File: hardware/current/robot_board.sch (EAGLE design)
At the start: 150 parts, among them J1 POWER_JACKPTH, Q1 DMP2035U, Q2 DMP2035U, Q3 DMP2035U-7, Q4 DMP2035U-7, Q5 DMP2035U, U1 FT232RL-BASICSSOP, U10 DRV8839, U12 LM393, U16 LM393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

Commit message: USB and main power are switched with on/off switch
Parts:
- removed D33: BAT54C, diode:BAT54C
- removed Q5: DMP2035U, jseng:DMP2035U
- added C13: 22uF, resistor:C-USC1206
- added R29: 330, resistor:R-US_R1206
- added R32: 20K 1%, resistor:R-US_R1206
- added R33: 300, resistor:R-US_R1206
- added U$5: AP431SAG-7, jseng:AP431SAG-7
- added U$6, U$7: SIA907EDJT, jseng:SIA907EDJT
- D23: value 2.4V -> RX; device SparkFun-DiscreteSemi:DIODESOT23 -> SparkFun-LED:LED-GREENLILYPAD
- JP4: device SparkFun-Connectors:M06SIP -> SparkFun-Connectors:M081X08
- R23: value 1K 1% -> 10K 1%
- R24: value 27K 1% -> 24K 1%
- R31: value 20K 1% -> 24K 1%
- R34: value 20K 1% -> 300
- R35: value 5.11K 1% -> 120K 1%
- R36: value 20K 1% -> 600K 1%
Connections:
- removed net 2.4V: D23.C, R23.1, U12G1.-IN, U12G2.-IN, U16G1.-IN
- removed net N$33: F1.2, JP4.6, Q1.D
- removed net N$36: Q1.G, R34.2
- new net 2.5V: R23.1, U$5.CATHODE, U$5.REF, U12G1.-IN, U12G2.-IN, U16G1.-IN
- new net N$22: D23.C, U1.TXLED
- new net N$23: U$7.D1, U$7.D2
- new net N$24: U$6.D1, U$6.D2
- new net N$25: R33.2, U$1.6
- new net N$26: R34.1, U$1.9
- new net PWR_GATE: Q1.D, R32.2, U$6.G1, U$6.G2
- new net VIN1: D24.A1, F1.2, U$6.S1
- net 3V3_OUT: now also JP4.4; no longer JP4.2
- net 5V: now also R29.1, U12G1.V+
- net 5V_OUT: now also JP4.5; no longer JP4.3
- net GND: now also C13.2, JP4.6, JP4.7, R32.1, U$5.ANODE; no longer D23.A, JP4.4, JP4.5, R34.1
- net LCD0: now also R34.2; no longer U$1.9
- net N$12: now also D23.A, R29.2; no longer D33.CC, R42.2
- net N$18: now also Q1.S, R42.2
- net N$7: now also JP4.3; no longer JP4.1
- net PWR_SW: now also U$6.S2, U$7.S2; no longer D33.A1, Q1.S, Q5.D
- net RS: now also R33.1; no longer U$1.6
- net USBGATE: now also Q1.G, U$7.G1, U$7.G2; no longer Q5.G, U$3.EN
- net USB_5V: now also U$7.S1; no longer D33.A2, Q5.S
- net VIN: now also R35.2
- net VIN_F: now also C13.1, JP4.8, U$3.EN; no longer D24.A1, R35.2, U12G1.V+
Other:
- note removed: "Reverse Polarity Protection"
- moved on the sheet: D24, F1, J1, Q1, R23, R28, R34, R35, R36, R42, U16G1, U16G2

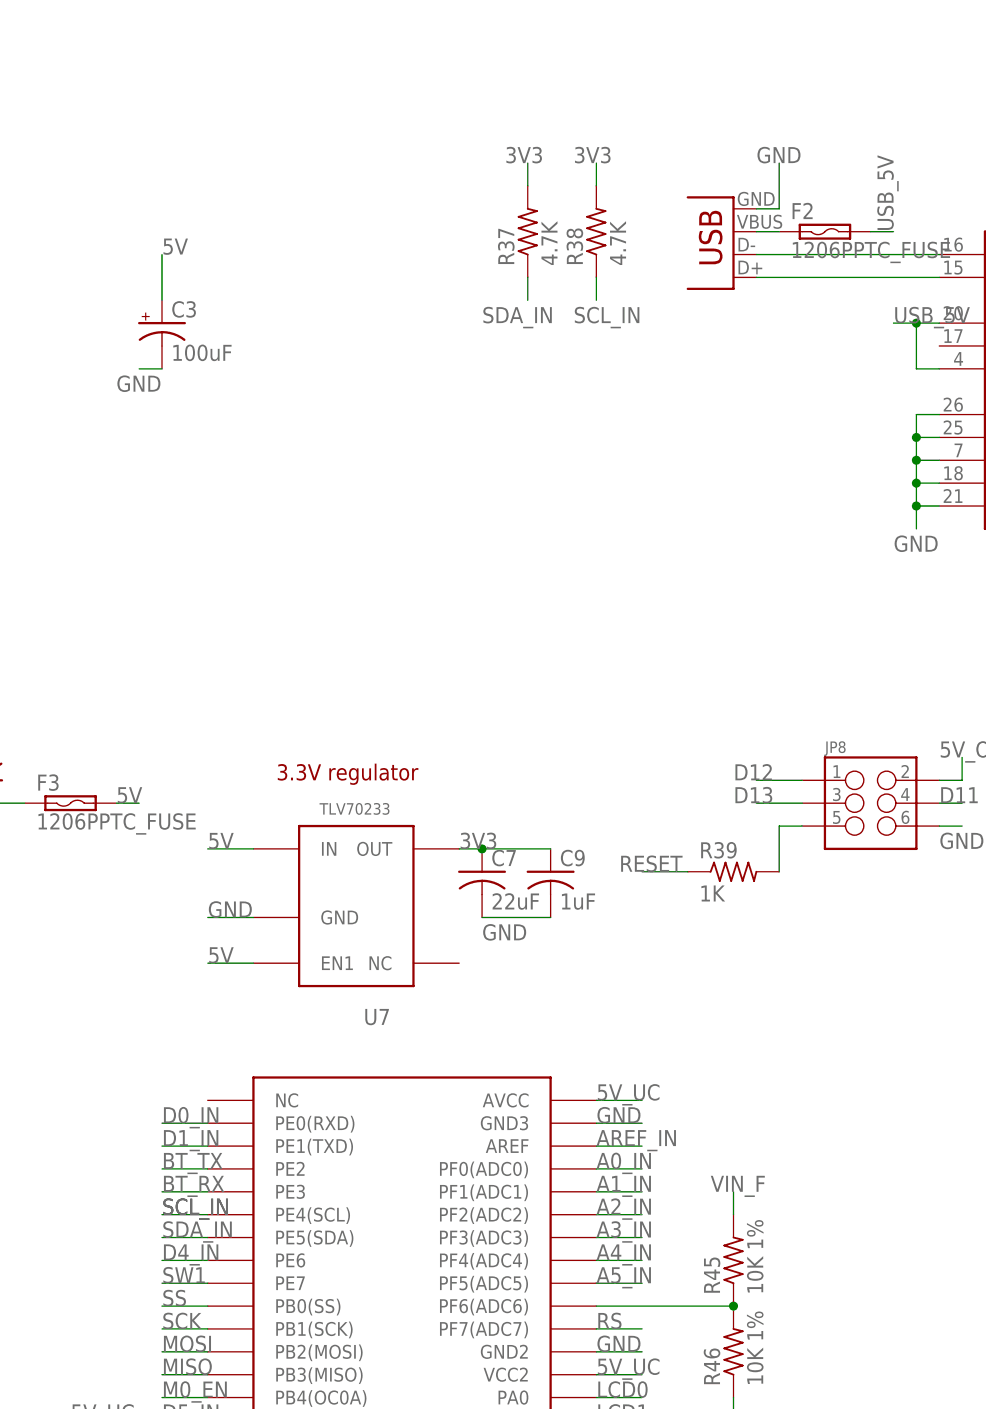
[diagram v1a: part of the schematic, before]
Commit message: added i2c level shifter
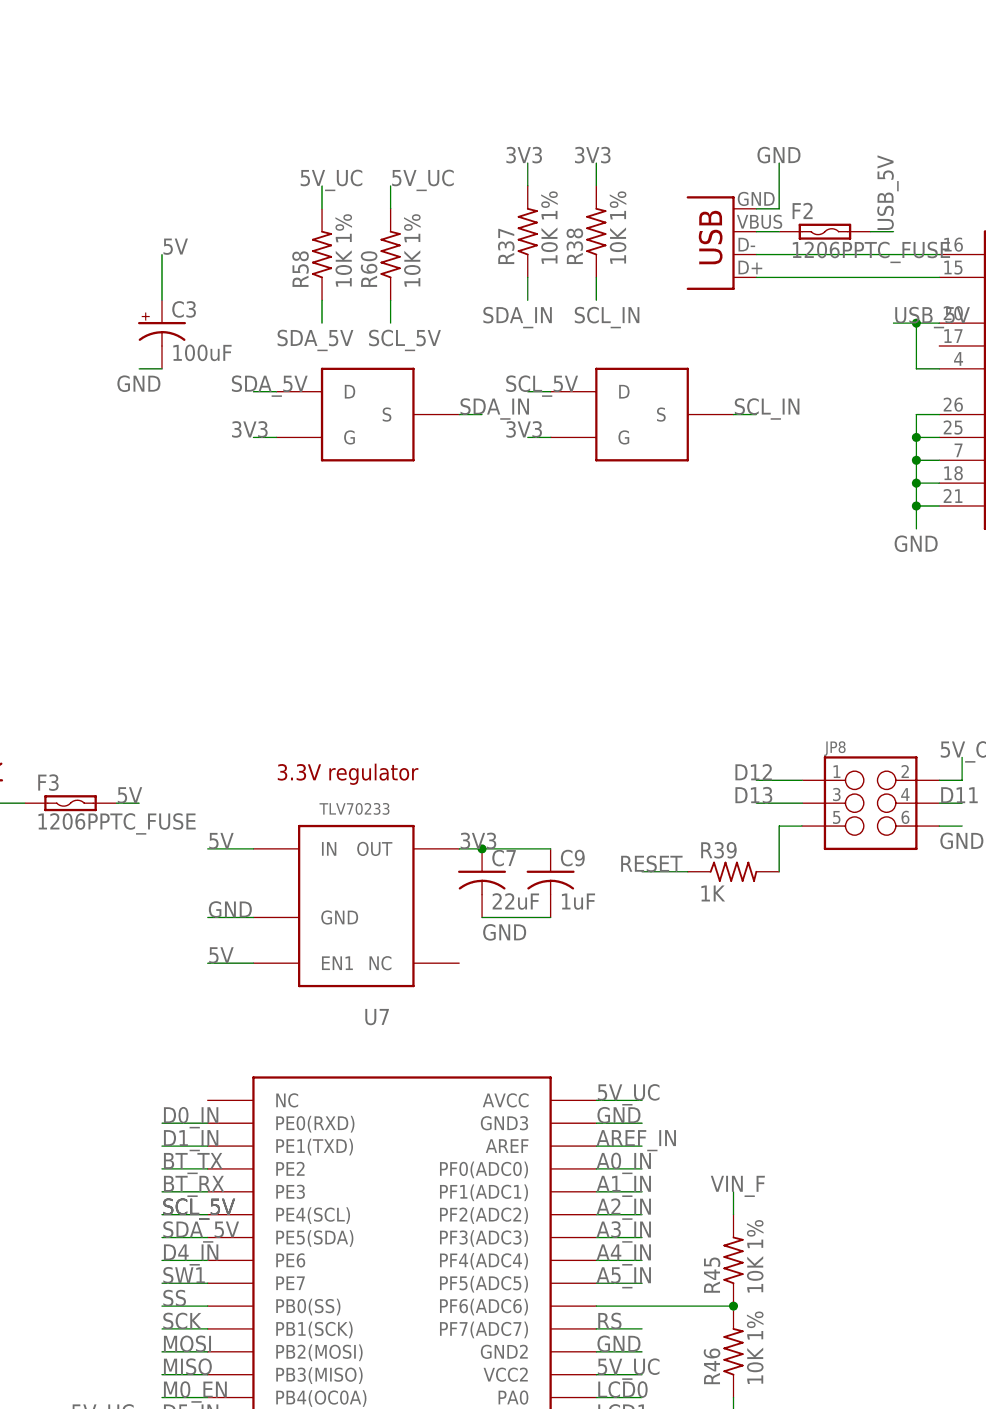
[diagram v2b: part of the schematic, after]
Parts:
- added R58, R60: 10K 1%, resistor:R-US_R1206
- added U$10, U$9: BSS138, jseng:BSS138
- R37, R38: value 4.7K -> 10K 1%
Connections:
- new net SCL_5V: R60.1, U$10.D, U17.PE4(SCL)
- new net SDA_5V: R58.1, U$9.D, U17.PE5(SDA)
- net 3V3: now also U$10.G, U$9.G
- net 5V_UC: now also R58.2, R60.2
- net SCL_IN: now also U$10.S; no longer U17.PE4(SCL)
- net SDA_IN: now also U$9.S; no longer U17.PE5(SDA)
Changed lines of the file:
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@@
 <part name="R30" library="resistor" deviceset="R-US_" device="R1206" value="20K 1%"/>
 <part name="R31" library="resistor" deviceset="R-US_" device="R1206" value="24K 1%"/>
-<part name="R37" library="resistor" deviceset="R-US_" device="R1206" value="4.7K"/>
-<part name="R38" library="resistor" deviceset="R-US_" device="R1206" value="4.7K"/>
+<part name="R37" library="resistor" deviceset="R-US_" device="R1206" value="10K 1%"/>
+<part name="R38" library="resistor" deviceset="R-US_" device="R1206" value="10K 1%"/>
 <part name="C4" library="resistor" deviceset="C-US" device="C1206" value=".1uF"/>
 <part name="R40" library="resistor" deviceset="R-US_" device="R1206" value="10K 1%"/>
@@
 <part name="R34" library="resistor" deviceset="R-US_" device="R1206" value="300"/>
 <part name="JP4" library="SparkFun-Connectors" deviceset="M08" device="1X08"/>
+<part name="R58" library="resistor" deviceset="R-US_" device="R1206" value="10K 1%"/>
+<part name="R60" library="resistor" deviceset="R-US_" device="R1206" value="10K 1%"/>
+<part name="U$9" library="jseng" deviceset="BSS138" device=""/>
+<part name="U$10" library="jseng" deviceset="BSS138" device=""/>
 </parts>
 <sheets>
@@
 <instance part="R34" gate="G$1" x="320.04" y="91.44" rot="R90"/>
 <instance part="JP4" gate="G$1" x="233.68" y="-45.72" rot="R180"/>
+<instance part="R58" gate="G$1" x="124.46" y="167.64" rot="R90"/>
+<instance part="R60" gate="G$1" x="132.08" y="167.64" rot="R90"/>
+<instance part="U$9" gate="G$1" x="129.54" y="149.86"/>
+<instance part="U$10" gate="G$1" x="160.02" y="149.86"/>
 </instances>
 <busses>
@@
 <label x="327.66" y="12.7" size="1.778" layer="95"/>
 </segment>
+<segment>
+<pinref part="U$9" gate="G$1" pin="G"/>
+<wire x1="119.38" y1="147.32" x2="116.84" y2="147.32" width="0.1524" layer="91"/>
+<label x="114.3" y="147.32" size="1.778" layer="95"/>
+</segment>
+<segment>
+<pinref part="U$10" gate="G$1" pin="G"/>
+<wire x1="149.86" y1="147.32" x2="147.32" y2="147.32" width="0.1524" layer="91"/>
+<label x="144.78" y="147.32" size="1.778" layer="95"/>
+</segment>
 </net>
 <net name="RESET" class="0">
@@
 <wire x1="335.28" y1="81.28" x2="332.74" y2="81.28" width="0.1524" layer="91"/>
 <label x="332.74" y="81.28" size="1.778" layer="95"/>
+</segment>
+<segment>
+<pinref part="R58" gate="G$1" pin="2"/>
+<wire x1="124.46" y1="172.72" x2="124.46" y2="175.26" width="0.1524" layer="91"/>
+<label x="121.92" y="175.26" size="1.778" layer="95"/>
+</segment>
+<segment>
+<pinref part="R60" gate="G$1" pin="2"/>
+<wire x1="132.08" y1="172.72" x2="132.08" y2="175.26" width="0.1524" layer="91"/>
+<label x="132.08" y="175.26" size="1.778" layer="95"/>
 </segment>
 </net>
@@
 <net name="SCL_IN" class="0">
 <segment>
-<pinref part="U17" gate="G$1" pin="PE4(SCL)"/>
-<wire x1="111.76" y1="60.96" x2="106.68" y2="60.96" width="0.1524" layer="91"/>
-<label x="106.68" y="60.96" size="1.778" layer="95"/>
-<label x="106.68" y="60.96" size="1.778" layer="95"/>
-</segment>
-<segment>
 <pinref part="D7" gate="G$1" pin="C"/>
 <pinref part="R7" gate="G$1" pin="1"/>
@@
 <label x="312.42" y="116.84" size="1.778" layer="95"/>
 </segment>
+<segment>
+<pinref part="U$10" gate="G$1" pin="S"/>
+<wire x1="170.18" y1="149.86" x2="172.72" y2="149.86" width="0.1524" layer="91"/>
+<label x="170.18" y="149.86" size="1.778" layer="95"/>
+</segment>
 </net>
 <net name="SDA_IN" class="0">
-<segment>
-<pinref part="U17" gate="G$1" pin="PE5(SDA)"/>
-<wire x1="111.76" y1="58.42" x2="106.68" y2="58.42" width="0.1524" layer="91"/>
-<label x="106.68" y="58.42" size="1.778" layer="95"/>
-</segment>
 <segment>
 <pinref part="D8" gate="G$1" pin="C"/>
@@
 <wire x1="332.74" y1="104.14" x2="325.12" y2="104.14" width="0.1524" layer="91"/>
 <label x="322.58" y="104.14" size="1.778" layer="95"/>
+</segment>
+<segment>
+<pinref part="U$9" gate="G$1" pin="S"/>
+<wire x1="139.7" y1="149.86" x2="142.24" y2="149.86" width="0.1524" layer="91"/>
+<label x="139.7" y="149.86" size="1.778" layer="95"/>
 </segment>
 </net>
@@
 </segment>
 </net>
+<net name="SCL_5V" class="0">
+<segment>
+<pinref part="U$10" gate="G$1" pin="D"/>
+<wire x1="149.86" y1="152.4" x2="147.32" y2="152.4" width="0.1524" layer="91"/>
+<label x="144.78" y="152.4" size="1.778" layer="95"/>
+</segment>
+<segment>
+<pinref part="R60" gate="G$1" pin="1"/>
+<wire x1="132.08" y1="162.56" x2="132.08" y2="160.02" width="0.1524" layer="91"/>
+<label x="129.54" y="157.48" size="1.778" layer="95"/>
+</segment>
+<segment>
+<pinref part="U17" gate="G$1" pin="PE4(SCL)"/>
+<wire x1="111.76" y1="60.96" x2="106.68" y2="60.96" width="0.1524" layer="91"/>
+<label x="106.68" y="60.96" size="1.778" layer="95"/>
+<label x="106.68" y="60.96" size="1.778" layer="95"/>
+</segment>
+</net>
+<net name="SDA_5V" class="0">
+<segment>
+<pinref part="U$9" gate="G$1" pin="D"/>
+<wire x1="119.38" y1="152.4" x2="116.84" y2="152.4" width="0.1524" layer="91"/>
+<label x="114.3" y="152.4" size="1.778" layer="95"/>
+</segment>
+<segment>
+<pinref part="R58" gate="G$1" pin="1"/>
+<wire x1="124.46" y1="162.56" x2="124.46" y2="160.02" width="0.1524" layer="91"/>
+<label x="119.38" y="157.48" size="1.778" layer="95"/>
+</segment>
+<segment>
+<pinref part="U17" gate="G$1" pin="PE5(SDA)"/>
+<wire x1="111.76" y1="58.42" x2="106.68" y2="58.42" width="0.1524" layer="91"/>
+<label x="106.68" y="58.42" size="1.778" layer="95"/>
+</segment>
+</net>

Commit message: revision 2
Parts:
- added JP12: M02PTH, SparkFun-Connectors:M02PTH
- added U$11: BSS138, jseng:BSS138
- R23: value 10K 1% -> 20K 1%
- U$1: value M08X2 -> 2X7HEADER; device SparkFun-Connectors:M08X2 -> jseng:2X7HEADER
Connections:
- new net ACCEL_INT1: U$11.G, U$8.INT1
- net 5V: now also U$1.P$2; no longer U$1.4
- net 5V_OUT: now also JP4.2
- net ACCEL_INT: now also U$11.D; no longer U$8.INT1
- net E: now also U$1.P$6; no longer U$1.8
- net GND: now also U$1.P$1, U$1.P$5, U$11.S; no longer U$1.3, U$1.7
- net LCD1: now also U$1.P$8; no longer U$1.10
- net LCD2: now also U$1.P$9; no longer U$1.11
- net LCD3: now also U$1.P$10; no longer U$1.12
- net LCD4: now also U$1.P$11; no longer U$1.13
- net LCD5: now also U$1.P$12; no longer U$1.14
- net LCD6: now also U$1.P$13; no longer U$1.15
- net LCD7: now also U$1.P$14; no longer U$1.16
- net LED0: now also U17.PG1; no longer U17.PG0
- net LED1: now also U17.PG0; no longer U17.PG1
- net N$15: now also U$1.P$3; no longer U$1.5
- net N$25: now also U$1.P$4; no longer U$1.6
- net N$26: now also U$1.P$7; no longer U$1.9
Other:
- moved on the sheet: IR, R33, R34, U$2
